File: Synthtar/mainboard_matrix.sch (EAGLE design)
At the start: 79 parts, among them IC1 74HC164N, IC2 4081N, IC3 555, IC4 4081N, J1 AUDIO_JACK_3.5MM_PTH, M1 ARDUINO-NANO-3.0, X1 HD44780LCD-1602, X2 MINI-USB-UX60A-MB-5ST

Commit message: more uploads
more recent files. code improvements
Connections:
- net GND: now also M1.GND.2, X1.RW
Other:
- note removed: "128x32=4096 bits (monochrome) 4096 bits/8 bits per byte = .5kB 1/2kB RAM Buffer needed to drive this"
- note removed: "may need to swap it out later"
- note removed: "right now I have a cheap 128x32 display that's super small (.96")"
- moved on the sheet: M1, R1, R3, U$6, X1

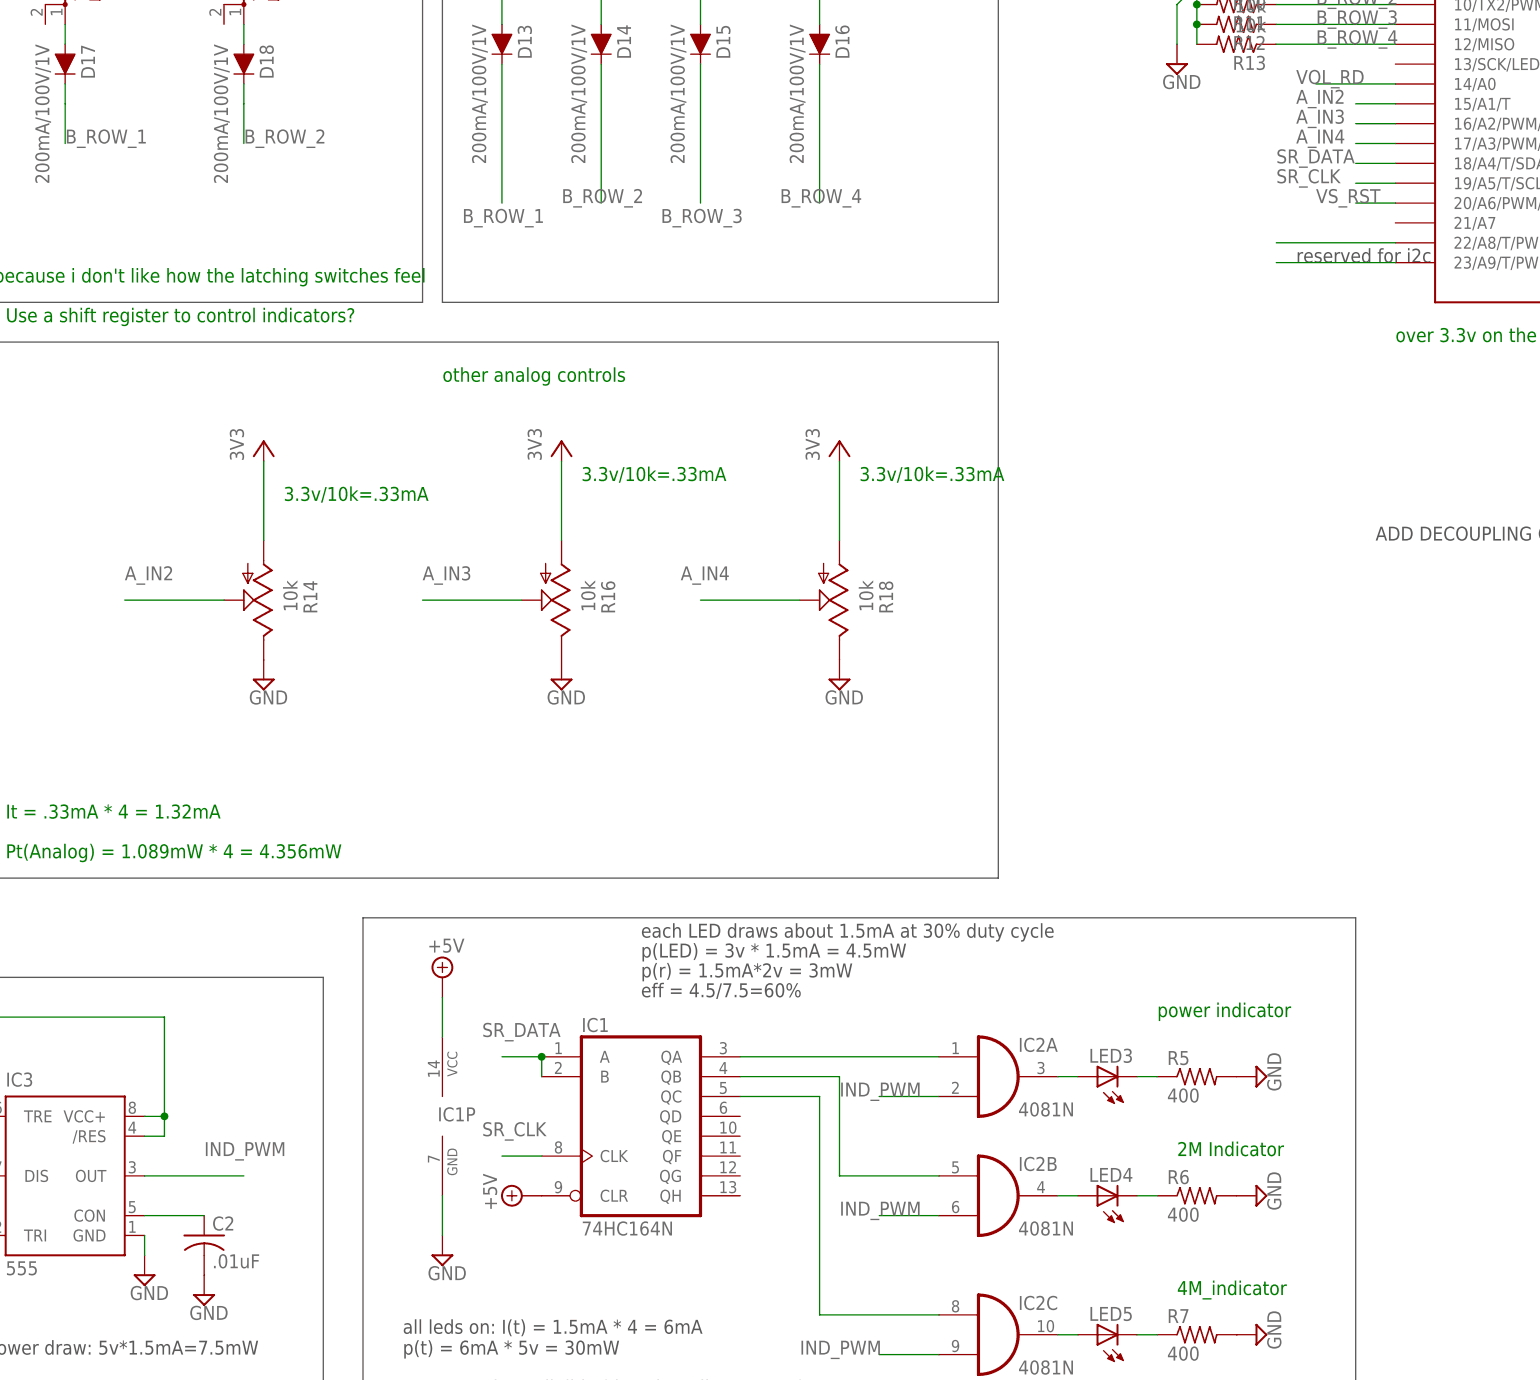
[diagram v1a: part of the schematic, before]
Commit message: Board building
started migrating overall schematic into individual boards
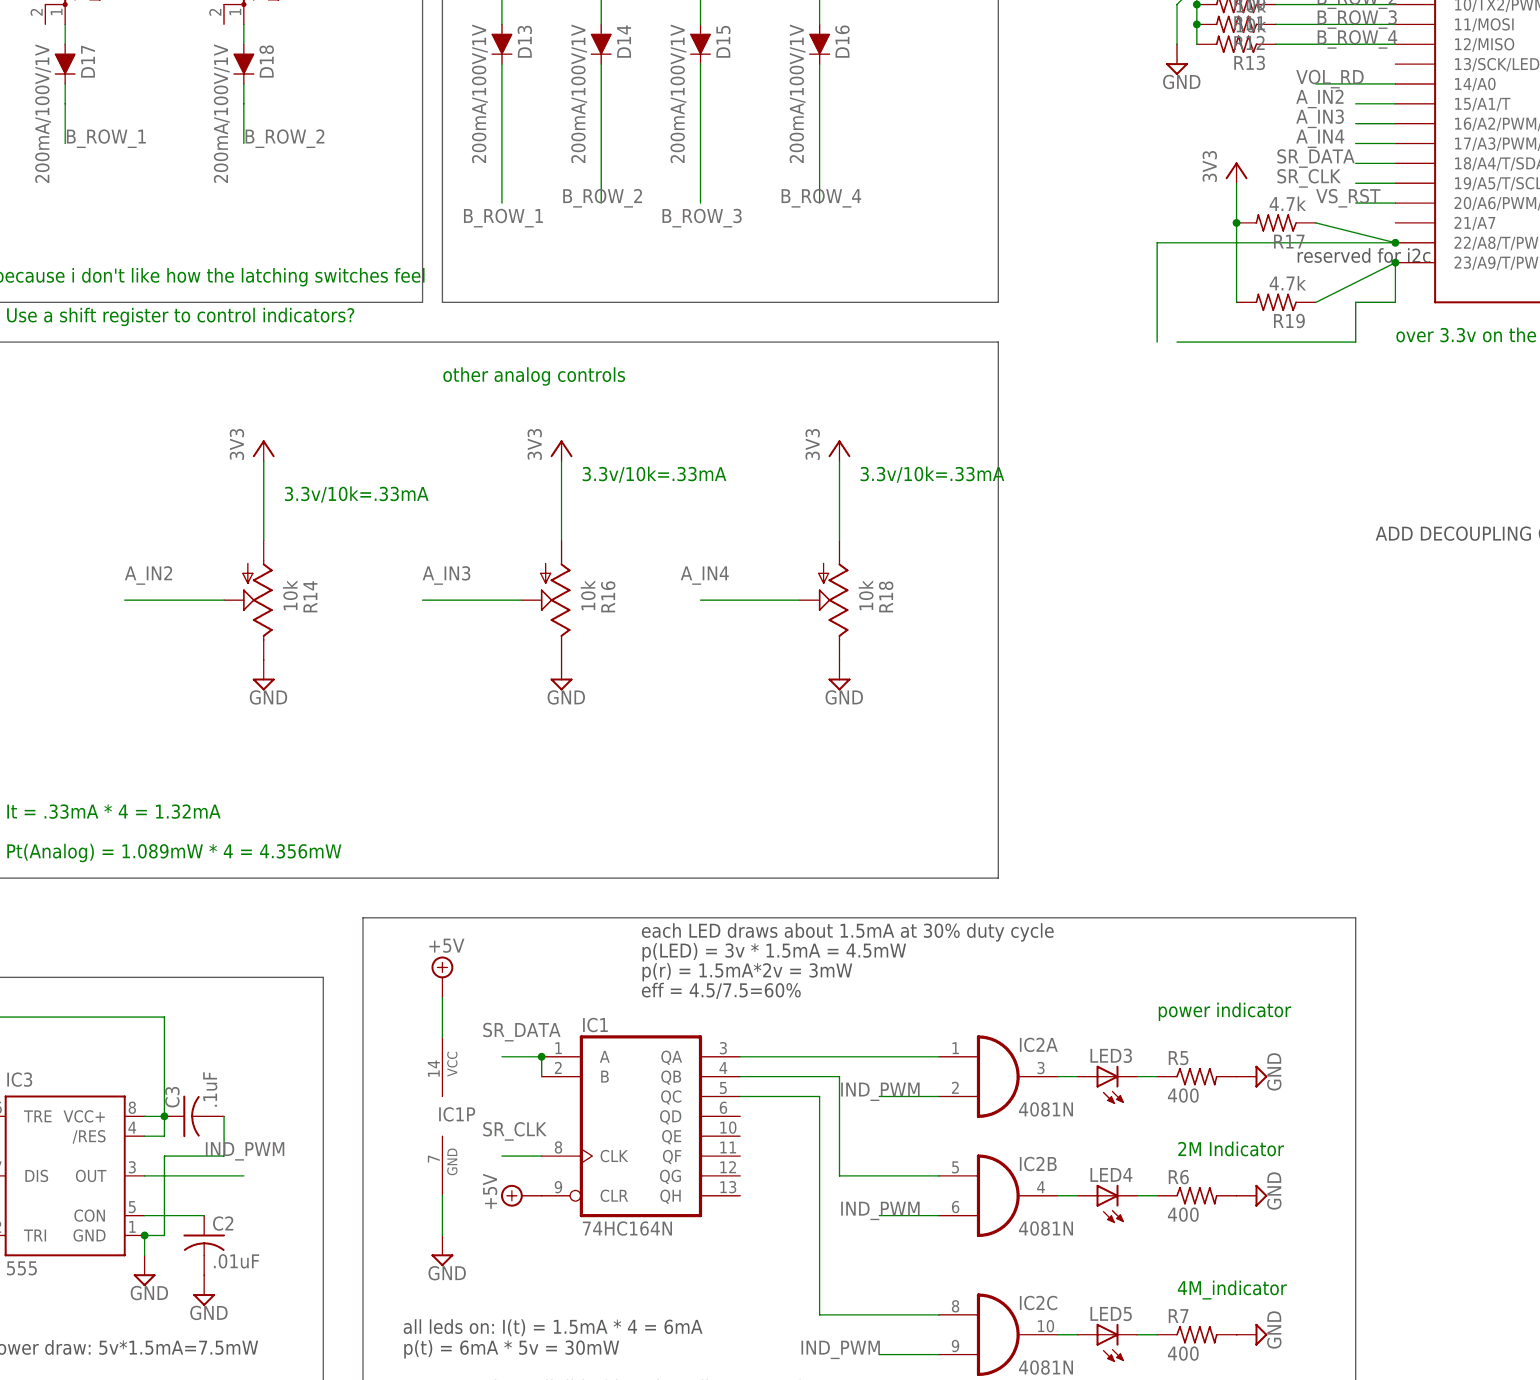
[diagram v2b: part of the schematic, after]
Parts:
- added C3: .1uF, rcl:C-US025-030X050
- added R17, R19: 4.7k, rcl:R-US_0204/7
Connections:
- net GND: now also C3.2
- net N$10: now also R17.1
- net N$65: now also C3.1
- net N$8: now also R19.1
- net VCC: now also R17.2, R19.2
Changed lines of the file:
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@@
 <part name="SUPPLY40" library="supply2" library_urn="urn:adsk.eagle:library:372" deviceset="GND" device=""/>
 <part name="SUPPLY41" library="supply2" library_urn="urn:adsk.eagle:library:372" deviceset="GND" device=""/>
+<part name="R17" library="rcl" library_urn="urn:adsk.eagle:library:334" deviceset="R-US_" device="0204/7" package3d_urn="urn:adsk.eagle:package:23498/1" value="4.7k"/>
+<part name="R19" library="rcl" library_urn="urn:adsk.eagle:library:334" deviceset="R-US_" device="0204/7" package3d_urn="urn:adsk.eagle:package:23498/1" value="4.7k"/>
+<part name="P+3" library="supply1" library_urn="urn:adsk.eagle:library:371" deviceset="VCC" device="" value="3V3"/>
+<part name="C3" library="rcl" library_urn="urn:adsk.eagle:library:334" deviceset="C-US" device="025-030X050" package3d_urn="urn:adsk.eagle:package:23631/1" value=".1uF"/>
 </parts>
 <sheets>
@@
 <instance part="SUPPLY40" gate="GND" x="-33.02" y="-38.1"/>
 <instance part="SUPPLY41" gate="GND" x="-7.62" y="-5.08" rot="R180"/>
+<instance part="R17" gate="G$1" x="-149.86" y="81.28" rot="R180"/>
+<instance part="R19" gate="G$1" x="-149.86" y="71.12" rot="R180"/>
+<instance part="P+3" gate="VCC" x="-154.94" y="88.9"/>
+<instance part="C3" gate="G$1" x="-289.56" y="-33.02" rot="R90"/>
 </instances>
 <busses>
@@
 <wire x1="-71.12" y1="10.16" x2="-66.04" y2="10.16" width="0.1524" layer="91"/>
 </segment>
+<segment>
+<pinref part="R17" gate="G$1" pin="2"/>
+<pinref part="P+3" gate="VCC" pin="VCC"/>
+<wire x1="-154.94" y1="86.36" x2="-154.94" y2="81.28" width="0.1524" layer="91"/>
+<pinref part="R19" gate="G$1" pin="2"/>
+<wire x1="-154.94" y1="71.12" x2="-154.94" y2="81.28" width="0.1524" layer="91"/>
+<junction x="-154.94" y="81.28"/>
+</segment>
 </net>
 <net name="GND" class="0">
@@
 <pinref part="SUPPLY31" gate="GND" pin="GND"/>
 <wire x1="-294.64" y1="-50.8" x2="-294.64" y2="-48.26" width="0.1524" layer="91"/>
+<wire x1="-294.64" y1="-48.26" x2="-292.1" y2="-48.26" width="0.1524" layer="91"/>
+<wire x1="-292.1" y1="-48.26" x2="-292.1" y2="-38.1" width="0.1524" layer="91"/>
+<junction x="-294.64" y="-48.26"/>
+<wire x1="-292.1" y1="-38.1" x2="-284.48" y2="-38.1" width="0.1524" layer="91"/>
+<pinref part="C3" gate="G$1" pin="2"/>
+<wire x1="-284.48" y1="-38.1" x2="-284.48" y2="-33.02" width="0.1524" layer="91"/>
 </segment>
 <segment>
@@
 <segment>
 <pinref part="U$5" gate="G$1" pin="23/A9/T/PWM/SDA1"/>
-<wire x1="-149.86" y1="76.2" x2="-134.62" y2="76.2" width="0.1524" layer="91"/>
+<wire x1="-144.78" y1="71.12" x2="-134.62" y2="76.2" width="0.1524" layer="91"/>
+<pinref part="R19" gate="G$1" pin="1"/>
+<wire x1="-134.62" y1="76.2" x2="-134.62" y2="71.12" width="0.1524" layer="91"/>
+<wire x1="-134.62" y1="71.12" x2="-139.7" y2="71.12" width="0.1524" layer="91"/>
+<junction x="-134.62" y="76.2"/>
+<wire x1="-139.7" y1="71.12" x2="-139.7" y2="66.04" width="0.1524" layer="91"/>
+<wire x1="-139.7" y1="66.04" x2="-162.56" y2="66.04" width="0.1524" layer="91"/>
 </segment>
 </net>
@@
 <wire x1="-347.98" y1="-27.94" x2="-347.98" y2="-20.32" width="0.1524" layer="91"/>
 <wire x1="-347.98" y1="-20.32" x2="-292.1" y2="-20.32" width="0.1524" layer="91"/>
+<pinref part="IC3" gate="G$1" pin="VCC+"/>
 <wire x1="-292.1" y1="-20.32" x2="-292.1" y2="-33.02" width="0.1524" layer="91"/>
-<pinref part="IC3" gate="G$1" pin="VCC+"/>
 <wire x1="-292.1" y1="-33.02" x2="-294.64" y2="-33.02" width="0.1524" layer="91"/>
 <pinref part="IC3" gate="G$1" pin="/RES"/>
@@
 <wire x1="-292.1" y1="-35.56" x2="-292.1" y2="-33.02" width="0.1524" layer="91"/>
 <junction x="-292.1" y="-33.02"/>
+<pinref part="C3" gate="G$1" pin="1"/>
 </segment>
 </net>
@@
 <segment>
 <pinref part="U$5" gate="G$1" pin="22/A8/T/PWM/SCL1"/>
-<wire x1="-134.62" y1="78.74" x2="-149.86" y2="78.74" width="0.1524" layer="91"/>
-</segment>
-</net>
+<wire x1="-134.62" y1="78.74" x2="-144.78" y2="81.28" width="0.1524" layer="91"/>
+<pinref part="R17" gate="G$1" pin="1"/>
+<junction x="-134.62" y="78.74"/>
+<wire x1="-134.62" y1="78.74" x2="-165.1" y2="78.74" width="0.1524" layer="91"/>
+<wire x1="-165.1" y1="78.74" x2="-165.1" y2="66.04" width="0.1524" layer="91"/>
+</segment>
+</net>

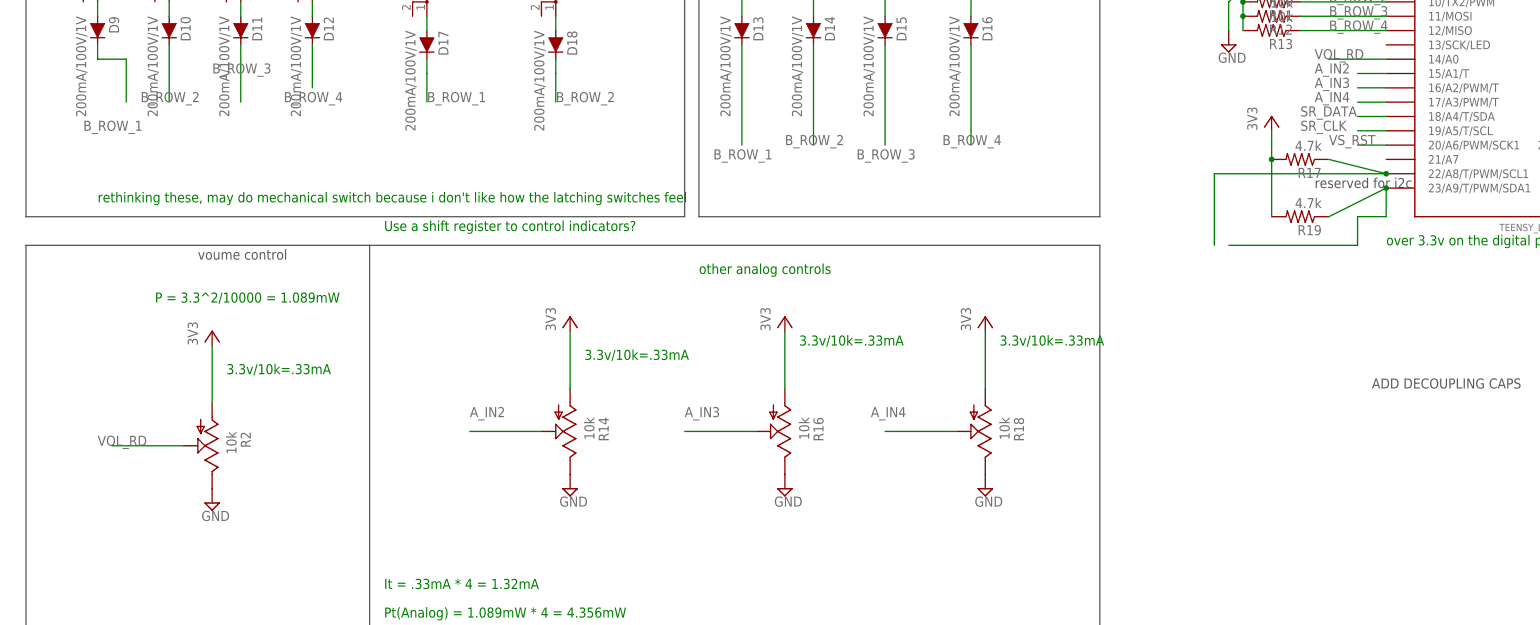
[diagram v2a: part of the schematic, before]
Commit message: Whammy Bar!
Finally added whammy bar, an old ps3 analog stick
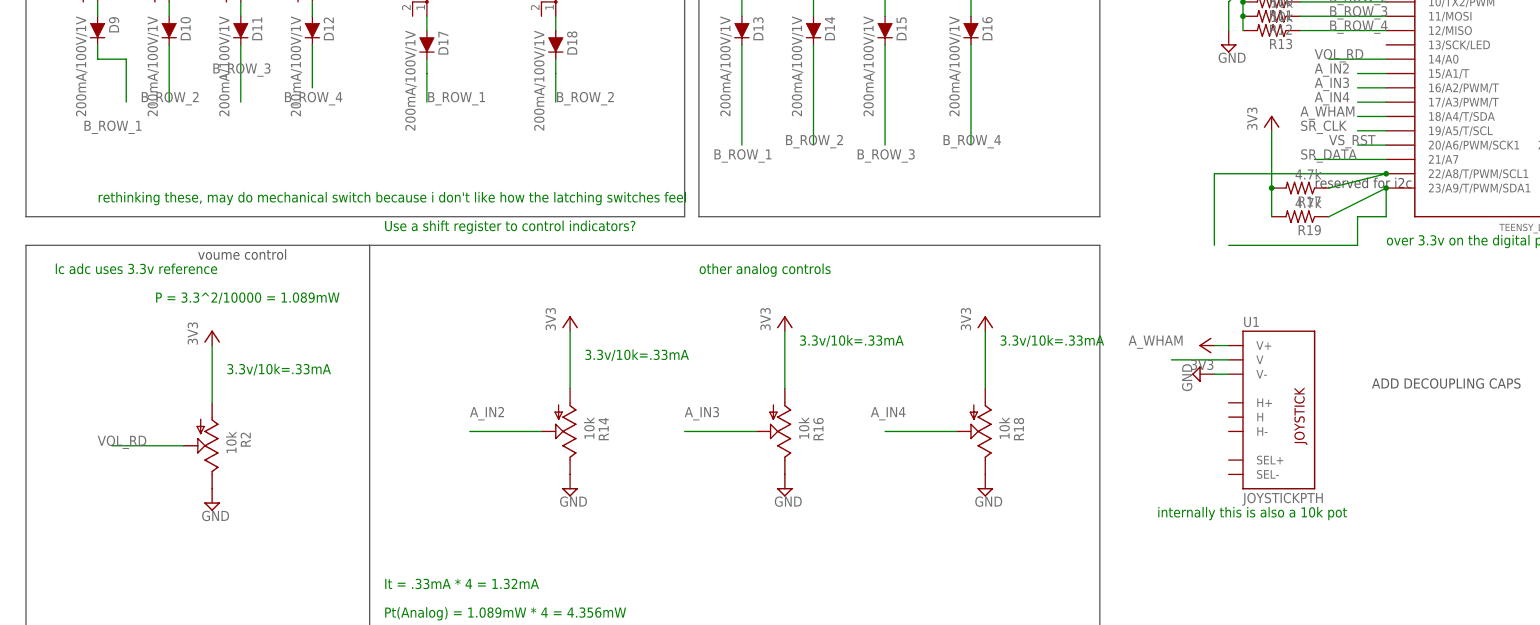
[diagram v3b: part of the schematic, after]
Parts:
- added U1: JOYSTICKPTH, adafruit:JOYSTICKPTH
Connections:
- new net A_WHAM: U$5.18/A4/T/SDA, U1.V
- net GND: now also U1.V-
- net SR_DATA: now also U$5.21/A7; no longer U$5.18/A4/T/SDA
- net VCC: now also U1.V+
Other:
- note added: "internally this is also a 10k pot"
- note added: "lc adc uses 3.3v reference"
- moved on the sheet: R17
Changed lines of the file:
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@@
 <part name="P+3" library="supply1" library_urn="urn:adsk.eagle:library:371" deviceset="VCC" device="" value="3V3"/>
 <part name="C3" library="rcl" library_urn="urn:adsk.eagle:library:334" deviceset="C-US" device="025-030X050" package3d_urn="urn:adsk.eagle:package:23631/1" value=".1uF"/>
+<part name="U1" library="adafruit" library_urn="urn:adsk.eagle:library:420" deviceset="JOYSTICK" device="PTH" package3d_urn="urn:adsk.eagle:package:6240846/1"/>
+<part name="P+5" library="supply1" library_urn="urn:adsk.eagle:library:371" deviceset="VCC" device="" value="3V3"/>
+<part name="SUPPLY42" library="supply2" library_urn="urn:adsk.eagle:library:372" deviceset="GND" device=""/>
 </parts>
 <sheets>
@@
 <text x="22.86" y="0" size="1.778" layer="91" rot="R90">backlight power</text>
 <wire x1="134.62" y1="10.16" x2="35.56" y2="10.16" width="0.1524" layer="97"/>
+<text x="-370.84" y="60.96" size="1.778" layer="91">lc adc uses 3.3v reference</text>
+<text x="-175.26" y="17.78" size="1.778" layer="91">internally this is also a 10k pot</text>
 </plain>
 <instances>
@@
 <instance part="SUPPLY40" gate="GND" x="-33.02" y="-38.1"/>
 <instance part="SUPPLY41" gate="GND" x="-7.62" y="-5.08" rot="R180"/>
-<instance part="R17" gate="G$1" x="-149.86" y="81.28" rot="R180"/>
+<instance part="R17" gate="G$1" x="-149.86" y="76.2" rot="R180"/>
 <instance part="R19" gate="G$1" x="-149.86" y="71.12" rot="R180"/>
 <instance part="P+3" gate="VCC" x="-154.94" y="88.9"/>
 <instance part="C3" gate="G$1" x="-289.56" y="-33.02" rot="R90"/>
+<instance part="U1" gate="G$1" x="-152.4" y="38.1"/>
+<instance part="P+5" gate="VCC" x="-167.64" y="48.26" rot="R90"/>
+<instance part="SUPPLY42" gate="GND" x="-167.64" y="43.18" rot="R270"/>
 </instances>
 <busses>
@@
 <pinref part="R17" gate="G$1" pin="2"/>
 <pinref part="P+3" gate="VCC" pin="VCC"/>
-<wire x1="-154.94" y1="86.36" x2="-154.94" y2="81.28" width="0.1524" layer="91"/>
+<wire x1="-154.94" y1="86.36" x2="-154.94" y2="76.2" width="0.1524" layer="91"/>
 <pinref part="R19" gate="G$1" pin="2"/>
-<wire x1="-154.94" y1="71.12" x2="-154.94" y2="81.28" width="0.1524" layer="91"/>
-<junction x="-154.94" y="81.28"/>
+<wire x1="-154.94" y1="71.12" x2="-154.94" y2="76.2" width="0.1524" layer="91"/>
+<junction x="-154.94" y="76.2"/>
+</segment>
+<segment>
+<pinref part="U1" gate="G$1" pin="V+"/>
+<pinref part="P+5" gate="VCC" pin="VCC"/>
+<wire x1="-165.1" y1="48.26" x2="-162.56" y2="48.26" width="0.1524" layer="91"/>
 </segment>
 </net>
@@
 <pinref part="X1" gate="G$1" pin="RW"/>
 </segment>
+<segment>
+<pinref part="U1" gate="G$1" pin="V-"/>
+<pinref part="SUPPLY42" gate="GND" pin="GND"/>
+<wire x1="-165.1" y1="43.18" x2="-162.56" y2="43.18" width="0.1524" layer="91"/>
+</segment>
 </net>
 <net name="+5V" class="0">
@@
 <net name="SR_DATA" class="0">
 <segment>
-<pinref part="U$5" gate="G$1" pin="18/A4/T/SDA"/>
-<wire x1="-134.62" y1="88.9" x2="-139.7" y2="88.9" width="0.1524" layer="91"/>
-<label x="-149.86" y="88.9" size="1.778" layer="95"/>
-</segment>
-<segment>
 <pinref part="IC1" gate="A" pin="B"/>
 <pinref part="IC1" gate="A" pin="A"/>
@@
 <junction x="-243.84" y="-25.4"/>
 <label x="-251.46" y="-22.86" size="1.778" layer="95"/>
+</segment>
+<segment>
+<pinref part="U$5" gate="G$1" pin="21/A7"/>
+<wire x1="-134.62" y1="81.28" x2="-147.32" y2="81.28" width="0.1524" layer="91"/>
+<label x="-149.86" y="81.28" size="1.778" layer="95"/>
 </segment>
 </net>
@@
 <segment>
 <pinref part="U$5" gate="G$1" pin="22/A8/T/PWM/SCL1"/>
-<wire x1="-134.62" y1="78.74" x2="-144.78" y2="81.28" width="0.1524" layer="91"/>
+<wire x1="-134.62" y1="78.74" x2="-144.78" y2="76.2" width="0.1524" layer="91"/>
 <pinref part="R17" gate="G$1" pin="1"/>
 <junction x="-134.62" y="78.74"/>
@@
 </segment>
 </net>
+<net name="A_WHAM" class="0">
+<segment>
+<pinref part="U1" gate="G$1" pin="V"/>
+<wire x1="-162.56" y1="45.72" x2="-172.72" y2="45.72" width="0.1524" layer="91"/>
+<label x="-180.34" y="48.26" size="1.778" layer="95"/>
+</segment>
+<segment>
+<pinref part="U$5" gate="G$1" pin="18/A4/T/SDA"/>
+<wire x1="-134.62" y1="88.9" x2="-139.7" y2="88.9" width="0.1524" layer="91"/>
+<label x="-149.86" y="88.9" size="1.778" layer="95"/>
+</segment>
+</net>
